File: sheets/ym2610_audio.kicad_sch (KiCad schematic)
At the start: 51 parts, among them J3 SMK S-G8043, U25 NJM2016D, U26 YM3016D, U27 YM2610, U28 PC4741, U29 PC4741

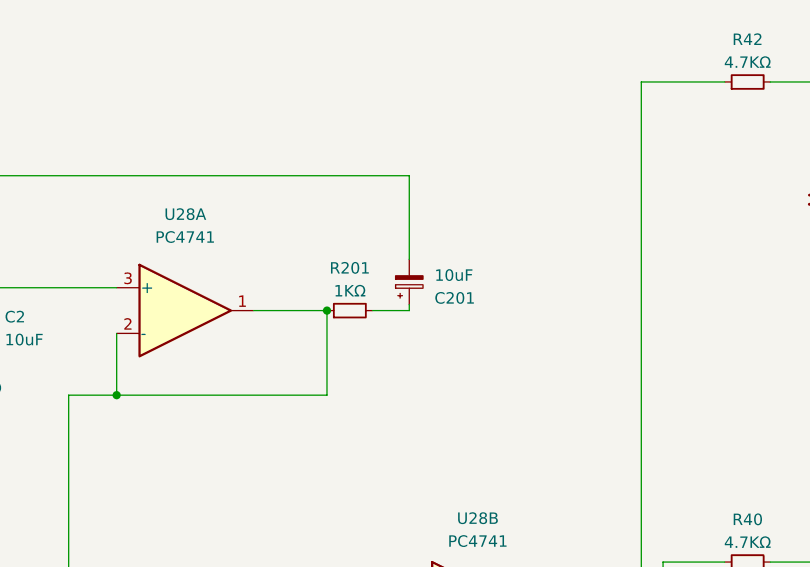
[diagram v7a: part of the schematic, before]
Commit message: Component Naming Corrections
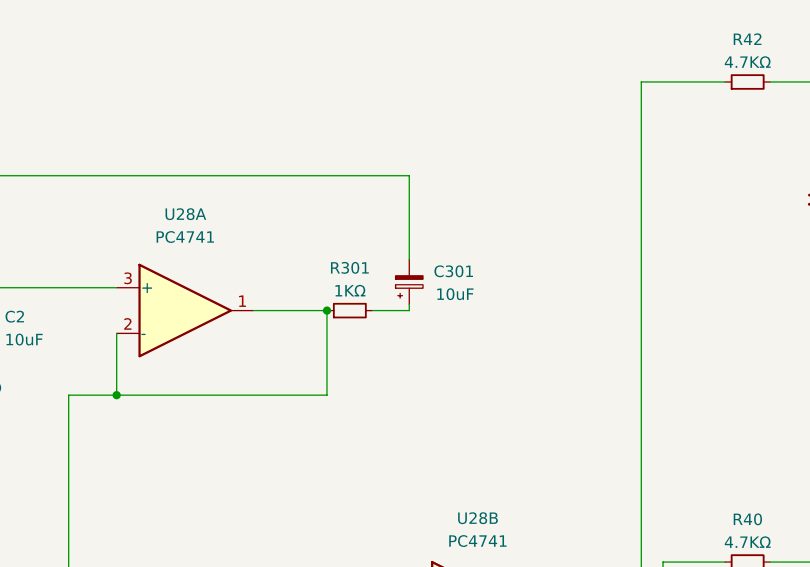
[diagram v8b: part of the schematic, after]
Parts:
- renumbered C201 to C301, R201 to R301
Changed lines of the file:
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@@
   )
   (symbol (lib_id "Device:C_Polarized_Small") (at 233.426 50.546 0) (mirror x) (unit 1)
-    (in_bom yes) (on_board yes) (fields_autoplaced)
-    (property "Reference" "C201" (id 0) (at 236.22 52.3622 0)
-      (effects (font (size 1.27 1.27)) (justify left))
-    )
-    (property "Value" "10uF" (id 1) (at 236.22 49.8222 0)
-      (effects (font (size 1.27 1.27)) (justify left))
+    (in_bom yes) (on_board yes)
+    (property "Reference" "C301" (id 0) (at 240.665 49.403 0)
+      (effects (font (size 1.27 1.27)) (justify right))
+    )
+    (property "Value" "10uF" (id 1) (at 240.665 51.943 0)
+      (effects (font (size 1.27 1.27)) (justify right))
     )
     (property "Footprint" "1_NeoGeoLibrary:CAP1-5mm" (id 2) (at 233.426 50.546 0)
@@
   (symbol (lib_id "Device:R_Small") (at 226.822 53.721 90) (unit 1)
     (in_bom yes) (on_board yes)
-    (property "Reference" "R201" (id 0) (at 226.822 49.022 90))
+    (property "Reference" "R301" (id 0) (at 226.822 49.022 90))
     (property "Value" "1KΩ" (id 1) (at 226.822 51.562 90))
     (property "Footprint" "1_NeoGeoLibrary:Resistor1-5mm" (id 2) (at 226.822 53.721 0)
